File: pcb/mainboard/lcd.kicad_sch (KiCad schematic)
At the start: 15 parts

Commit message: - Upgrade KiCad to latest version - Working on PM circuits - Initial USB Type-C support - Initial support for LCD
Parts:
- added C? (x3): 100nF, symbol Device:C
- added J?: Conn_01x40_MountingPin, symbol Connector_Generic_MountingPin:Conn_01x40_MountingPin
- added R?: 22K, Resistor_SMD:R_0402_1005Metric, symbol Device:R
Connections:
- net +3V3: now also C?.1, J?.38 (Pin_38), J?.39 (Pin_39)
- net GND: now also C?.2, C?.2, C?.2, J?.1 (Pin_1), J?.10 (Pin_10), J?.13 (Pin_13), J?.16 (Pin_16), J?.17 (Pin_17), J?.27 (Pin_27), J?.30 (Pin_30), J?.32 (Pin_32), J?.33 (Pin_33), J?.37 (Pin_37), J?.4 (Pin_4), J?.7 (Pin_7), J?.MP (MountPin)
- new net: C?.1, J?.24 (Pin_24), R?.2
- new net +1V8: C?.1, J?.18 (Pin_18), J?.19 (Pin_19), R?.1
- new net LCD_LEDA: J?.35 (Pin_35), J?.36 (Pin_36)
- new net LCD_LEDK: J?.28 (Pin_28), J?.29 (Pin_29)
- new net MIPI_TX0_CKN: J?.9 (Pin_9)
- new net MIPI_TX0_CKP: J?.8 (Pin_8)
- new net MIPI_TX0_D0N: J?.3 (Pin_3)
- new net MIPI_TX0_D0P: J?.2 (Pin_2)
- new net MIPI_TX0_D1N: J?.6 (Pin_6)
- new net MIPI_TX0_D1P: J?.5 (Pin_5)
- new net MIPI_TX0_D2N: J?.12 (Pin_12)
- new net MIPI_TX0_D2P: J?.11 (Pin_11)
- new net MIPI_TX0_D3N: J?.15 (Pin_15)
- new net MIPI_TX0_D3P: J?.14 (Pin_14)
- no-connect marks 0 -> 9
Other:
- note added: "LED: 6S2P, 18V @ 100mA"
- moved on the sheet: C?, J?, U?

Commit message: - pcb: working on r0p1 sch
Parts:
- removed C? (x8): 10pF, symbol Device:C
- removed C?: 100nF, symbol Device:C
- removed J?: Conn_01x30_Shielded, symbol Connector_Generic_Shielded:Conn_01x30_Shielded
- removed R?: 22K, Resistor_SMD:R_0402_1005Metric, symbol Device:R
- added C? (x9): 220nF, Capacitor_SMD:C_0402_1005Metric, symbol Device:C
- added C? (x2): 22uF, Capacitor_SMD:C_0603_1608Metric, symbol Device:C
- added C? (x2): 18pF, Capacitor_SMD:C_0603_1608Metric, symbol Device:C
- added C?: 1uF/35V, Capacitor_SMD:C_0603_1608Metric, symbol Device:C
- added C?: 100nF, Capacitor_SMD:C_0402_1005Metric, symbol Device:C
- added C?: 10uF, Capacitor_SMD:C_0603_1608Metric, symbol Device:C
- added D?: MBR0530, Diode_SMD:D_SOD-123, symbol Diode:MBR0530
- added J?: Conn_01x06_MountingPin, symbol Connector_Generic_MountingPin:Conn_01x06_MountingPin
- added J?: Conn_01x28_MountingPin, symbol Connector_Generic_MountingPin:Conn_01x28_MountingPin
- added J?: Conn_01x40_MountingPin, symbol Connector_Generic_MountingPin:Conn_01x40_MountingPin
- added L?: 22uH, Inductor_SMD:L_Vishay_IHLP-1212, symbol Device:L
- added R? (x3): 4.7K, Resistor_SMD:R_0402_1005Metric, symbol Device:R
- added R? (x2): 10K, Resistor_SMD:R_0402_1005Metric, symbol Device:R
- added R?: 3R, Resistor_SMD:R_0402_1005Metric, symbol Device:R
- added R?: 1K, Resistor_SMD:R_0402_1005Metric, symbol Device:R
- added R?: 49.9K/1%, Resistor_SMD:R_0402_1005Metric, symbol Device:R
- added U?: DS90C385A, Package_SO:TSSOP-56_6.1x14mm_P0.5mm, symbol symbols:DS90C385A
- added U?: CAT4139, Package_TO_SOT_SMD:SOT-23-5, symbol Regulator_Switching:AP3012
- added U?: SSD2828, Package_DFN_QFN:QFN-68-1EP_8x8mm_P0.4mm_EP5.2x5.2mm_ThermalVias, symbol symbols:SSD2828
- added Y?: 24MHz, Crystal:Crystal_SMD_3225-4Pin_3.2x2.5mm, symbol Device:Crystal_GND24
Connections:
- net +1V8: now also C?.1, C?.1, C?.1, C?.1, C?.1, U?.16 (VDDIO), U?.33 (VDDIO), U?.64 (VDDIO), U?.68 (VDDIO)
- net +3V3: now also J?.27 (Pin_27), J?.28 (Pin_28), J?.3 (Pin_3), J?.39 (Pin_39), J?.40 (Pin_40), R?.1, U?.1 (VCC), U?.26 (VCC), U?.34 (PLL_VCC), U?.44 (LVDS_VCC), U?.9 (VCC)
- net +5V: now also C?.2, C?.2, J?.1 (Pin_1), J?.2 (Pin_2), J?.37 (Pin_37), J?.38 (Pin_38), L?.1, U?.5 (IN)
- net GND: now also C?.1, C?.1, C?.1, C?.1, C?.1, C?.1, C?.2, C?.2, C?.2, C?.2, C?.2, C?.2, C?.2, C?.2, C?.2, C?.2, J?.1 (Pin_1), J?.10 (Pin_10), J?.12 (Pin_12), J?.15 (Pin_15), J?.18 (Pin_18), J?.19 (Pin_19), J?.21 (Pin_21), J?.23 (Pin_23), J?.24 (Pin_24), J?.26 (Pin_26), J?.28 (Pin_28), J?.3 (Pin_3), J?.30 (Pin_30), J?.36 (Pin_36), J?.6 (Pin_6), J?.6 (Pin_6), J?.9 (Pin_9), J?.MP (MountPin), J?.MP (MountPin), J?.MP (MountPin), R?.1, R?.1, R?.2, R?.2, U?.12 (GND), U?.13 (GND), U?.2 (GND), U?.21 (GND), U?.25 (TxIN23), U?.27 (SHUT), U?.27 (TxIN24), U?.28 (TxIN25), U?.29 (GND), U?.3 (GND), U?.30 (TxIN26), U?.32 (GND), U?.33 (PLL_GND), U?.35 (PLL_GND), U?.36 (LVDS_GND), U?.43 (LVDS_GND), U?.49 (LVDS_GND), U?.5 (GND), U?.50 (TxIN27), U?.53 (GND), U?.6 (GND), U?.65 (GND), U?.67 (GND), U?.69 (EP), U?.9 (GND), Y?.2, Y?.4
- net LCD1_RESET: now reaches J?.24 (Pin_24)
- net LCD1_RESET: now also J?.4 (Pin_4), U?.22 (RESET)
- net LCD_LEDA renamed LEDA
- net LEDA: now also C?.2, D?.1 (K)
- net LCD_LEDK renamed LEDK
- net LEDK: now also R?.1, R?.1
- net MIPI_TX0_CKN renamed MIPI_CN
- net MIPI_CN: now also U?.8 (MIPI_CN)
- net MIPI_TX0_CKP renamed MIPI_CP
- net MIPI_CP: now also U?.7 (MIPI_CP)
- net MIPI_TX0_D0N renamed MIPI_DN0
- net MIPI_DN0: now also U?.2 (MIPI_DN0)
- net MIPI_TX0_D0P renamed MIPI_DP0
- net MIPI_DP0: now also U?.1 (MIPI_DP0)
- net MIPI_TX0_D1N renamed MIPI_DN1
- net MIPI_DN1: now also U?.5 (MIPI_DN1)
- net MIPI_TX0_D1P renamed MIPI_DP1
- net MIPI_DP1: now also U?.4 (MIPI_DP1)
- net MIPI_TX0_D2N renamed MIPI_DN2
- net MIPI_DN2: now also U?.11 (MIPI_DN2)
- net MIPI_TX0_D2P renamed MIPI_DP2
- net MIPI_DP2: now also U?.10 (MIPI_DP2)
- net MIPI_TX0_D3N renamed MIPI_DN3
- net MIPI_DN3: now also U?.14 (MIPI_DN3)
- net MIPI_TX0_D3P renamed MIPI_DP3
- net MIPI_DP3: now also U?.13 (MIPI_DP3)
- new net: R?.2, U?.18 (PS1)
- new net: R?.2, U?.17 (R_FB)
- new net: D?.2 (A), L?.2, U?.1 (SW)
- new net: R?.1, R?.2, U?.3 (FB)
- new net: C?.2, R?.1, R?.2
- new net: C?.2, U?.63 (TX_CLK_XIN), Y?.3
- new net: C?.2, U?.62 (TX_CLK_XIO), Y?.1
- new net: R?.2, U?.17 (PS0)
- new net +1V2: C?.1, C?.1, C?.1, C?.1, C?.1, U?.15 (MVDD), U?.31 (MVDD), U?.60 (MVDD), U?.66 (MVDD)
- new net EPDC_BDR0: J?.27 (Pin_27), U?.24 (TxIN22)
- new net EPDC_D0: J?.2 (Pin_2), U?.51 (TxIN0)
- new net EPDC_D1: J?.3 (Pin_3), U?.52 (TxIN1)
- new net EPDC_D10: J?.13 (Pin_13), U?.8 (TxIN10)
- new net EPDC_D11: J?.14 (Pin_14), U?.10 (TxIN11)
- new net EPDC_D12: J?.15 (Pin_15), U?.11 (TxIN12)
- new net EPDC_D13: J?.16 (Pin_16), U?.12 (TxIN13)
- new net EPDC_D14: J?.17 (Pin_17), U?.14 (TxIN14)
- new net EPDC_D15: J?.18 (Pin_18), U?.15 (TxIN15)
- new net EPDC_D2: J?.4 (Pin_4), U?.54 (TxIN2)
- new net EPDC_D3: J?.5 (Pin_5), U?.55 (TxIN3)
- new net EPDC_D4: J?.6 (Pin_6), U?.56 (TxIN4)
- new net EPDC_D5: J?.7 (Pin_7), U?.2 (TxIN5)
- new net EPDC_D6: J?.8 (Pin_8), U?.3 (TxIN6)
- new net EPDC_D7: J?.9 (Pin_9), U?.4 (TxIN7)
- new net EPDC_D8: J?.11 (Pin_11), U?.6 (TxIN8)
- new net EPDC_D9: J?.12 (Pin_12), U?.7 (TxIN9)
- new net EPDC_GDCLK: J?.24 (Pin_24), U?.20 (TxIN19)
- new net EPDC_GDOE: J?.25 (Pin_25), U?.22 (TxIN20)
- new net EPDC_GDSP: J?.26 (Pin_26), U?.23 (TxIN21)
- new net EPDC_PWRSTAT: J?.32 (Pin_32), J?.5 (Pin_5)
- new net EPDC_SDCE0: J?.20 (Pin_20), U?.16 (TxIN16)
- new net EPDC_SDCLK: J?.29 (Pin_29), U?.31 (TxCLKIN)
- new net EPDC_SDLE: J?.21 (Pin_21), U?.18 (TxIN17)
- new net EPDC_SDOE: J?.22 (Pin_22), U?.19 (TxIN18)
- new net EPD_PWR_EN: J?.31 (Pin_31), J?.4 (Pin_4), U?.32 (~PWR_DWN)
- new net EPD_TP_INT: J?.25 (Pin_25), J?.33 (Pin_33)
- new net I2C1_SCL: J?.1 (Pin_1)
- new net I2C1_SDA: J?.2 (Pin_2)
- new net I2C2_SCL: J?.23 (Pin_23), J?.35 (Pin_35)
- new net I2C2_SDA: J?.22 (Pin_22), J?.34 (Pin_34)
- new net LCD1_CLK: U?.30 (PCLK)
- new net LCD1_DE: U?.28 (DEN)
- new net LCD1_HSYNC: U?.29 (HSYNC)
- new net LCD1_VSYNC: U?.34 (VSYNC)
- new net LCD_D0: U?.35 (DATA0)
- new net LCD_D1: U?.36 (DATA1)
- new net LCD_D10: U?.45 (DATA10)
- new net LCD_D11: U?.46 (DATA11)
- new net LCD_D12: U?.47 (DATA12)
- new net LCD_D13: U?.48 (DATA13)
- new net LCD_D14: U?.49 (DATA14)
- new net LCD_D15: U?.50 (DATA15)
- new net LCD_D16: U?.51 (DATA16)
- new net LCD_D17: U?.52 (DATA17)
- new net LCD_D18: U?.53 (DATA18)
- new net LCD_D19: U?.54 (DATA19)
- new net LCD_D2: U?.37 (DATA2)
- new net LCD_D20: U?.55 (DATA20)
- new net LCD_D21: U?.56 (DATA21)
- new net LCD_D22: U?.57 (DATA22)
- new net LCD_D23: U?.58 (DATA23)
- new net LCD_D3: U?.38 (DATA3)
- new net LCD_D4: U?.39 (DATA4)
- new net LCD_D5: U?.40 (DATA5)
- new net LCD_D6: U?.41 (DATA6)
- new net LCD_D7: U?.42 (DATA7)
- new net LCD_D8: U?.43 (DATA8)
- new net LCD_D9: U?.44 (DATA9)
- new net LCD_EN: R?.1, U?.4 (~SHDN~)
- new net LCD_PWM: R?.2
- new net LCD_TP_INT: J?.5 (Pin_5)
- new net LVDS_CKN: J?.11 (Pin_11), U?.40 (TxCLKOUT-)
- new net LVDS_CKP: J?.10 (Pin_10), U?.39 (TxCLKOUT+)
- new net LVDS_D0N: J?.20 (Pin_20), U?.48 (TxOUT0-)
- new net LVDS_D0P: J?.19 (Pin_19), U?.47 (TxOUT0+)
- new net LVDS_D1N: J?.17 (Pin_17), U?.46 (TxOUT1-)
- new net LVDS_D1P: J?.16 (Pin_16), U?.45 (TxOUT1+)
- new net LVDS_D2N: J?.14 (Pin_14), U?.42 (TxOUT2-)
- new net LVDS_D2P: J?.13 (Pin_13), U?.41 (TxOUT2+)
- new net LVDS_D3N: J?.8 (Pin_8), U?.38 (TxOUT3-)
- new net LVDS_D3P: J?.7 (Pin_7), U?.37 (TxOUT3+)
- new net SPI_LCD_CS: U?.59 (CSX)
- new net SPI_LCD_MISO: U?.23 (SDO)
- new net SPI_LCD_MOSI: U?.24 (SDI)
- new net SPI_LCD_SCLK: U?.25 (SCK)
- no-connect marks 9 -> 14
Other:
- note added: "Addr 0xBB/0xBA"
- note added: "Alternative Connector Bypassing LVDS SerDes"
- moved on the sheet: C?, J?, U?

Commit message: - pcb: r0p1 sch draft
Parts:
- gave numbers to parts that had none: 42

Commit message: - pcb: start r0p1 layout
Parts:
- added C524, C525, C526, C527: 220nF, Capacitor_SMD:C_0402_1005Metric, symbol Device:C
- added C528: 22uF, Capacitor_SMD:C_0603_1608Metric, symbol Device:C
- C509, C512, C519, C521, C522: footprint (none) -> Capacitor_SMD:C_0402_1005Metric
- C520, C523: footprint (none) -> Capacitor_SMD:C_0603_1608Metric
- J501, J503: footprint (none) -> Connector_FFC-FPC:Hirose_FH12-40S-0.5SH_1x40-1MP_P0.50mm_Horizontal
- J502: footprint (none) -> Connector_FFC-FPC:Hirose_FH12-6S-0.5SH_1x06-1MP_P0.50mm_Horizontal
- J504: footprint (none) -> Connector_FFC-FPC:Hirose_FH12-28S-0.5SH_1x28-1MP_P0.50mm_Horizontal
- R501, R502, R508: value 4.7K -> 10K
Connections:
- net +3V3: now also C524.1, C525.1, C526.1, C527.1, C528.1
- net GND: now also C524.2, C525.2, C526.2, C527.2, C528.2
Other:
- company: Copyright EI-2030 2021. -> Copyright EI-2030 2021. / Engineer: Wenting Zhang
- title: Archer -> Archer Mainboard

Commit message: - pcb: finishing layout r0p1
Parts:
- C502, C504: footprint Capacitor_SMD:C_0603_1608Metric -> Capacitor_SMD:C_0402_1005Metric
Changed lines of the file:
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@@
       (effects (font (size 1.27 1.27)) (justify left))
     )
-    (property "Footprint" "Capacitor_SMD:C_0603_1608Metric" (id 2) (at 91.1352 170.18 0)
+    (property "Footprint" "Capacitor_SMD:C_0402_1005Metric" (id 2) (at 91.1352 170.18 0)
       (effects (font (size 1.27 1.27)) hide)
     )
@@
       (effects (font (size 1.27 1.27)) (justify left))
     )
-    (property "Footprint" "Capacitor_SMD:C_0603_1608Metric" (id 2) (at 103.8352 170.18 0)
+    (property "Footprint" "Capacitor_SMD:C_0402_1005Metric" (id 2) (at 103.8352 170.18 0)
       (effects (font (size 1.27 1.27)) hide)
     )

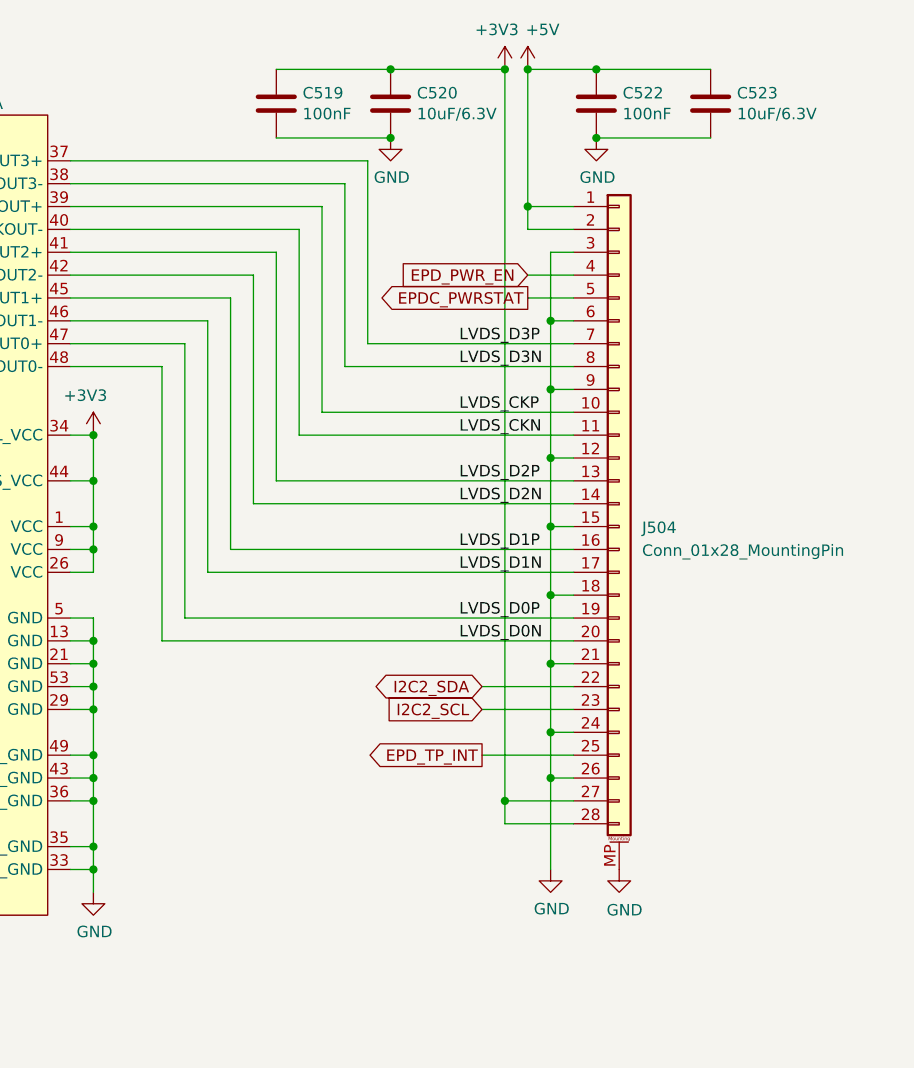
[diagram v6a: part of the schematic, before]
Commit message: - pcb: start working on screen board
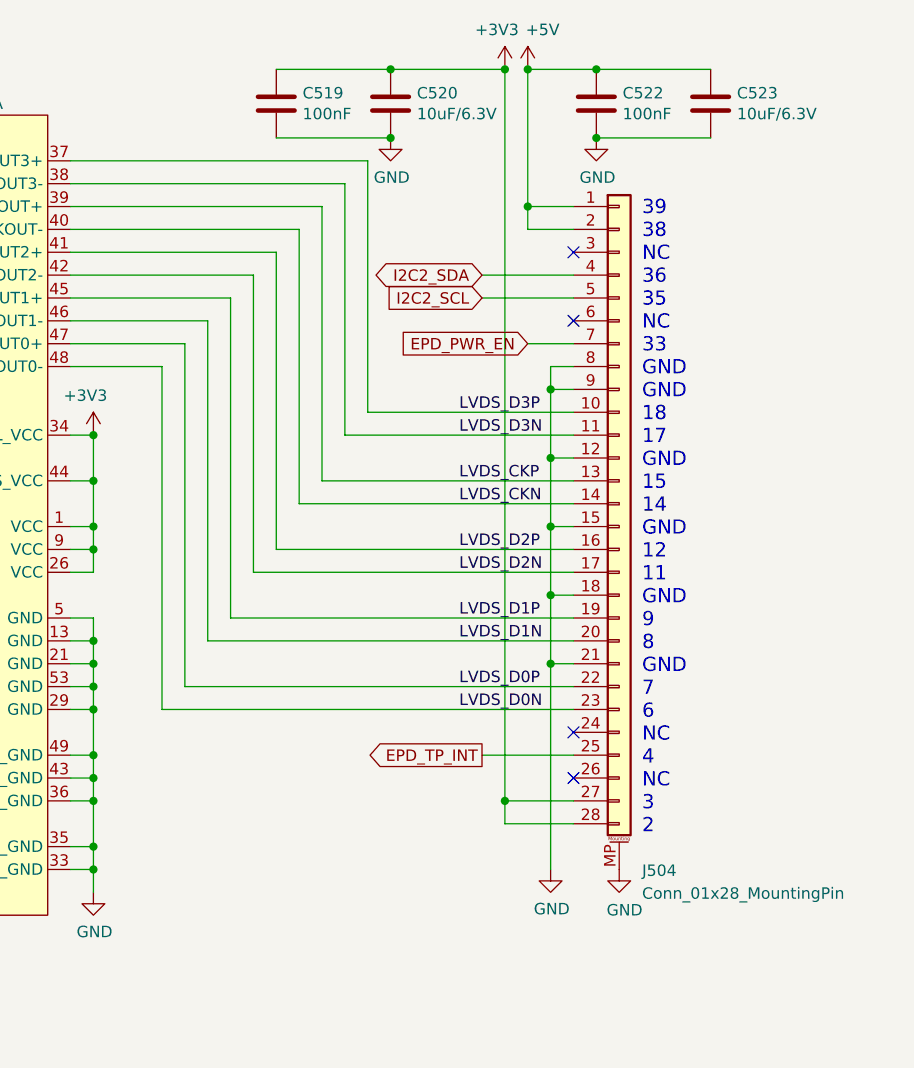
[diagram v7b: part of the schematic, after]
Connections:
- net EPDC_PWRSTAT: no longer J504.5 (Pin_5)
- net EPD_PWR_EN: now also J504.7 (Pin_7); no longer J504.4 (Pin_4)
- net GND: now also J504.8 (Pin_8); no longer J504.24 (Pin_24), J504.26 (Pin_26), J504.3 (Pin_3), J504.6 (Pin_6)
- net I2C2_SCL: now also J504.5 (Pin_5); no longer J504.23 (Pin_23)
- net I2C2_SDA: now also J504.4 (Pin_4); no longer J504.22 (Pin_22)
- net LVDS_CKN: now also J504.14 (Pin_14); no longer J504.11 (Pin_11)
- net LVDS_CKP: now also J504.13 (Pin_13); no longer J504.10 (Pin_10)
- net LVDS_D0N: now also J504.23 (Pin_23); no longer J504.20 (Pin_20)
- net LVDS_D0P: now also J504.22 (Pin_22); no longer J504.19 (Pin_19)
- net LVDS_D1N: now also J504.20 (Pin_20); no longer J504.17 (Pin_17)
- net LVDS_D1P: now also J504.19 (Pin_19); no longer J504.16 (Pin_16)
- net LVDS_D2N: now also J504.17 (Pin_17); no longer J504.14 (Pin_14)
- net LVDS_D2P: now also J504.16 (Pin_16); no longer J504.13 (Pin_13)
- net LVDS_D3N: now also J504.11 (Pin_11); no longer J504.8 (Pin_8)
- net LVDS_D3P: now also J504.10 (Pin_10); no longer J504.7 (Pin_7)
- no-connect marks 14 -> 18
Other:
- note added: "39 38 NC 36 35 NC 33 GND GND 18 17 GND 15 14 GND 12 11 GND 9 8 GND 7 6 NC 4 NC 3 2"
